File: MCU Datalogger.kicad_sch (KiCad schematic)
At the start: 25 parts, among them U1 24LC1025, U2 DS1337S_, U3 24LC1025, U4 ATMEGA328P-AU, Y1 32.768 MHz, Y2 16 MHz

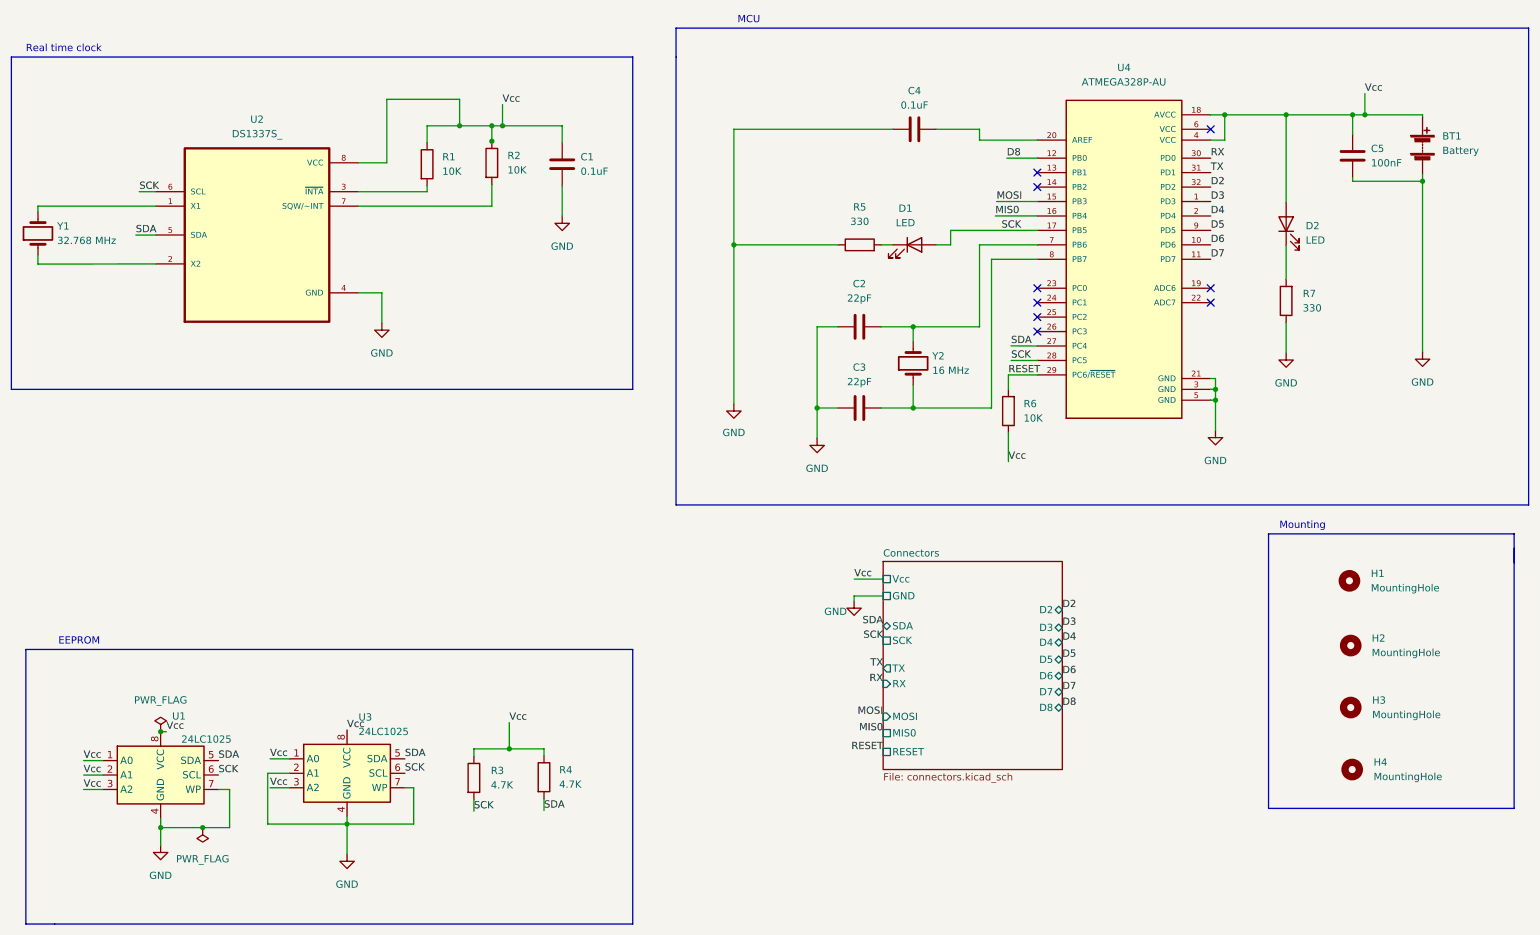
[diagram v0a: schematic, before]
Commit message: Fixed net bugs in 4 layer version of the PCB.
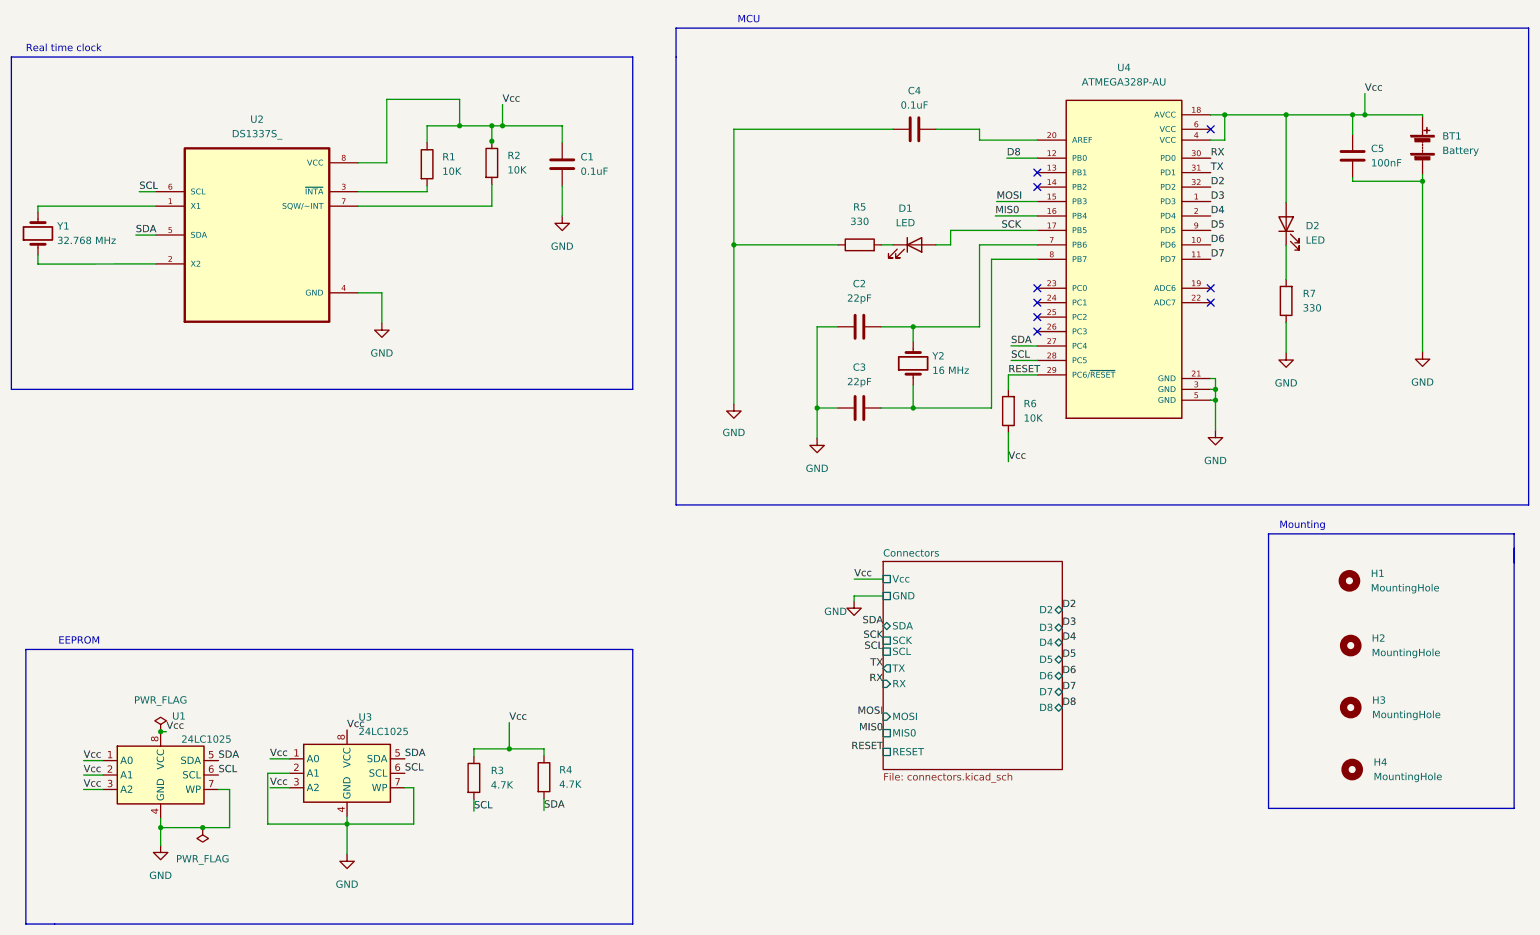
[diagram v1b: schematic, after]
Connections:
- net SCK: no longer R3.2, U1.6 (SCL), U2.6 (SCL), U3.6 (SCL), U4.28 (PC5)
- new net SCL: R3.2, U1.6 (SCL), U2.6 (SCL), U3.6 (SCL), U4.28 (PC5)
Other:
- sheet Connectors ports: added SCL; removed none
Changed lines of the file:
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@@
     (effects (font (size 1.27 1.27)) (justify left bottom))
   )
-  (label "SCK" (at 37.719 46.5328 0)
-    (effects (font (size 1.27 1.27)) (justify left bottom))
-  )
-  (label "SCK" (at 190.9826 76.2 0)
+  (label "SCL" (at 37.719 46.5328 0)
+    (effects (font (size 1.27 1.27)) (justify left bottom))
+  )
+  (label "SCL" (at 190.9826 76.2 0)
     (effects (font (size 1.27 1.27)) (justify left bottom))
   )
@@
     (effects (font (size 1.27 1.27)) (justify left bottom))
   )
-  (label "SCK" (at 51.6382 149.0726 0)
+  (label "SCL" (at 51.6382 149.0726 0)
     (effects (font (size 1.27 1.27)) (justify left bottom))
   )
@@
     (effects (font (size 1.27 1.27)) (justify left bottom))
   )
-  (label "SCK" (at 96.5454 155.4226 0)
-    (effects (font (size 1.27 1.27)) (justify left bottom))
+  (label "SCL" (at 96.5454 155.4226 0)
+    (effects (font (size 1.27 1.27)) (justify left bottom))
+  )
+  (label "SCL" (at 168.4782 127.381 180)
+    (effects (font (size 1.27 1.27)) (justify right bottom))
   )
   (label "SDA" (at 108.8644 155.2956 0)
@@
     (effects (font (size 1.27 1.27)) (justify right bottom))
   )
-  (label "SCK" (at 84.4042 148.7678 0)
+  (label "SCL" (at 84.4042 148.7678 0)
     (effects (font (size 1.27 1.27)) (justify left bottom))
   )
@@
       (effects (font (size 1.27 1.27)) (justify left))
     )
+    (pin "SCL" passive (at 168.4782 127.381 180)
+      (effects (font (size 1.27 1.27)) (justify left))
+    )
   )
   (sheet_instances
@@
       (reference "H4") (unit 1) (value "MountingHole") (footprint "MountingHole:MountingHole_2.1mm")
     )
-    (path "/1c9fce4d-fc04-4198-a681-89c79bd95e1b/655e3b4f-9164-467b-be5c-8412b1ba3bc3"
-      (reference "J1") (unit 1) (value "Conn_01x04_Male") (footprint "Connector_PinHeader_2.54mm:PinHeader_1x04_P2.54mm_Vertical")
-    )
-    (path "/1c9fce4d-fc04-4198-a681-89c79bd95e1b/d8f39dba-e152-4788-9498-f518c1ce42f1"
-      (reference "J2") (unit 1) (value "Conn_01x09_Male") (footprint "Connector_PinHeader_2.54mm:PinHeader_1x09_P2.54mm_Vertical")
-    )
-    (path "/1c9fce4d-fc04-4198-a681-89c79bd95e1b/3a2c9243-fcbd-4b43-95f2-7f23cfb4b426"
-      (reference "J3") (unit 1) (value "Conn_01x04_Male") (footprint "Connector_PinHeader_2.54mm:PinHeader_1x04_P2.54mm_Vertical")
-    )
-    (path "/1c9fce4d-fc04-4198-a681-89c79bd95e1b/eb7c15ec-2c7f-4621-8bbb-1c40e4541887"
-      (reference "J4") (unit 1) (value "Conn_02x03_Odd_Even") (footprint "Connector_PinHeader_2.54mm:PinHeader_2x03_P2.54mm_Vertical")
+    (path "/1c9fce4d-fc04-4198-a681-89c79bd95e1b/35453001-c791-4af9-b30f-0e1476103394"
+      (reference "J?") (unit 1) (value "Conn_01x04_Male") (footprint "Connector_PinHeader_2.54mm:PinHeader_1x04_P2.54mm_Vertical")
+    )
+    (path "/1c9fce4d-fc04-4198-a681-89c79bd95e1b/45f3ee1c-49c2-40a8-8c61-15640f290546"
+      (reference "J?") (unit 1) (value "Conn_02x03_Odd_Even") (footprint "Connector_PinHeader_2.54mm:PinHeader_2x03_P2.54mm_Vertical")
+    )
+    (path "/1c9fce4d-fc04-4198-a681-89c79bd95e1b/c818d6fa-4612-4318-931d-9f096e9c4e85"
+      (reference "J?") (unit 1) (value "Conn_01x09_Male") (footprint "Connector_PinHeader_2.54mm:PinHeader_1x09_P2.54mm_Vertical")
+    )
+    (path "/1c9fce4d-fc04-4198-a681-89c79bd95e1b/e3dae971-9362-4f9b-8843-511fd47055b7"
+      (reference "J?") (unit 1) (value "Conn_01x04_Male") (footprint "Connector_PinHeader_2.54mm:PinHeader_1x04_P2.54mm_Vertical")
     )
     (path "/f9104431-c12b-4262-85a4-3fb81a6448ea"
